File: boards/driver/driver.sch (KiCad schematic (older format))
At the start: 0 parts

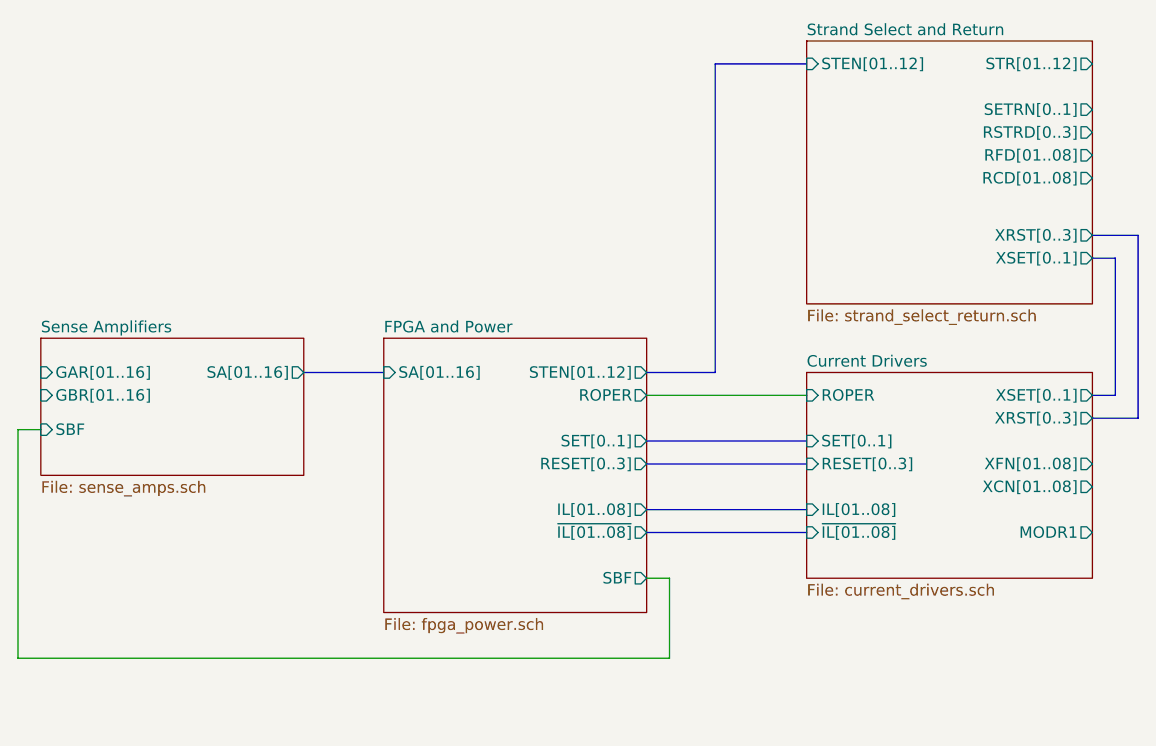
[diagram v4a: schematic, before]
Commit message: Completely overhauled rope driver circuitry to much, much more closely resemble the original.
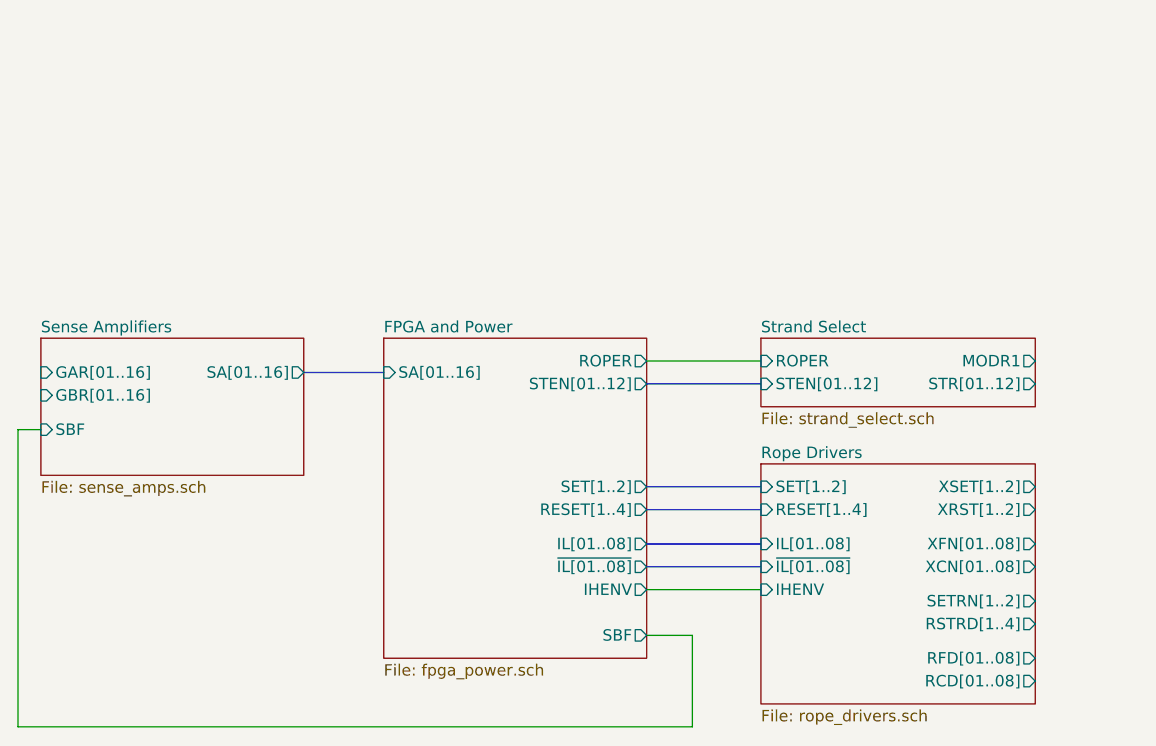
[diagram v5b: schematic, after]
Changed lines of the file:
@@
 $Descr USLedger 17000 11000
 encoding utf-8
-Sheet 1 5
+Sheet 1 68
 Title ""
 Date ""
@@
 F5 "SA[01..16]" O R 6950 3900 50
 $EndSheet
+Wire Bus Line
+	6950 3900 7300 3900
+Wire Wire Line
+	5700 4150 5800 4150
 $Sheet
-S 9150 2450 1250 1150
+S 8950 3750 1200 300
 U 64D2DF1E
-F0 "Strand Select and Return" 50
-F1 "strand_select_return.sch" 50
-F2 "STEN[01..12]" I L 9150 2550 50
-F3 "STR[01..12]" O R 10400 2550 50
-F4 "SETRN[0..1]" O R 10400 2750 50
-F5 "XSET[0..1]" O R 10400 3400 50
-F6 "RSTRD[0..3]" O R 10400 2850 50
-F7 "XRST[0..3]" O R 10400 3300 50
-F8 "RFD[01..08]" O R 10400 2950 50
-F9 "RCD[01..08]" O R 10400 3050 50
+F0 "Strand Select" 50
+F1 "strand_select.sch" 50
+F2 "STR[01..12]" O R 10150 3950 50
+F3 "ROPER" I L 8950 3850 50
+F4 "MODR1" O R 10150 3850 50
+F5 "STEN[01..12]" I L 8950 3950 50
 $EndSheet
 $Sheet
-S 9150 3900 1250 900
+S 8950 4300 1200 1050
 U 6183FAE6
-F0 "Current Drivers" 50
-F1 "current_drivers.sch" 50
-F2 "MODR1" O R 10400 4600 50
-F3 "ROPER" I L 9150 4000 50
-F4 "SET[0..1]" I L 9150 4200 50
-F5 "XSET[0..1]" O R 10400 4000 50
-F6 "RESET[0..3]" I L 9150 4300 50
-F7 "XRST[0..3]" O R 10400 4100 50
-F8 "~IL[01..08]" I L 9150 4600 50
-F9 "IL[01..08]" I L 9150 4500 50
-F10 "XFN[01..08]" O R 10400 4300 50
-F11 "XCN[01..08]" O R 10400 4400 50
+F0 "Rope Drivers" 50
+F1 "rope_drivers.sch" 50
+F2 "IHENV" I L 8950 4850 50
+F3 "SET[1..2]" I L 8950 4400 50
+F4 "RESET[1..4]" I L 8950 4500 50
+F5 "XRST[1..2]" O R 10150 4500 50
+F6 "XSET[1..2]" O R 10150 4400 50
+F7 "IL[01..08]" I L 8950 4650 50
+F8 "~IL[01..08]" I L 8950 4750 50
+F9 "XFN[01..08]" O R 10150 4650 50
+F10 "XCN[01..08]" O R 10150 4750 50
+F11 "RFD[01..08]" O R 10150 5150 50
+F12 "RCD[01..08]" O R 10150 5250 50
+F13 "SETRN[1..2]" O R 10150 4900 50
+F14 "RSTRD[1..4]" O R 10150 5000 50
 $EndSheet
+Wire Wire Line
+	8450 3850 8950 3850
 Wire Bus Line
-	10400 3300 10600 3300
-Wire Bus Line
-	10400 3400 10500 3400
-Wire Bus Line
-	10500 3400 10500 4000
-Wire Bus Line
-	10500 4000 10400 4000
+	8950 3950 8450 3950
 $Sheet
-S 7300 3750 1150 1200
+S 7300 3750 1150 1400
 U 652D8F7B
 F0 "FPGA and Power" 50
 F1 "fpga_power.sch" 50
 F2 "SA[01..16]" I L 7300 3900 50
-F3 "STEN[01..12]" O R 8450 3900 50
-F4 "SET[0..1]" O R 8450 4200 50
-F5 "RESET[0..3]" O R 8450 4300 50
-F6 "IL[01..08]" O R 8450 4500 50
-F7 "~IL[01..08]" O R 8450 4600 50
-F8 "ROPER" O R 8450 4000 50
-F9 "SBF" O R 8450 4800 50
+F3 "STEN[01..12]" O R 8450 3950 50
+F4 "SET[1..2]" O R 8450 4400 50
+F5 "RESET[1..4]" O R 8450 4500 50
+F6 "IL[01..08]" O R 8450 4650 50
+F7 "~IL[01..08]" O R 8450 4750 50
+F8 "ROPER" O R 8450 3850 50
+F9 "SBF" O R 8450 5050 50
+F10 "IHENV" O R 8450 4850 50
 $EndSheet
+Wire Wire Line
+	8450 4850 8950 4850
 Wire Bus Line
-	6950 3900 7300 3900
+	8450 4750 8950 4750
 Wire Bus Line
-	8450 3900 8750 3900
+	8950 4650 8450 4650
 Wire Bus Line
-	8750 3900 8750 2550
+	8450 4500 8950 4500
 Wire Bus Line
-	8750 2550 9150 2550
+	8950 4400 8450 4400
 Wire Wire Line
-	8450 4000 9150 4000
-Wire Bus Line
-	8450 4200 9150 4200
-Wire Bus Line
-	8450 4300 9150 4300
-Wire Bus Line
-	8450 4500 9150 4500
-Wire Bus Line
-	9150 4600 8450 4600
+	8450 5050 8650 5050
 Wire Wire Line
-	8450 4800 8550 4800
+	8650 5050 8650 5450
 Wire Wire Line
-	8550 4800 8550 5150
+	8650 5450 5700 5450
 Wire Wire Line
-	8550 5150 5700 5150
-Wire Wire Line
-	5700 5150 5700 4150
-Wire Wire Line
-	5700 4150 5800 4150
-Wire Bus Line
-	10400 4100 10600 4100
-Wire Bus Line
-	10600 3300 10600 4100
+	5700 4150 5700 5450
 $EndSCHEMATC

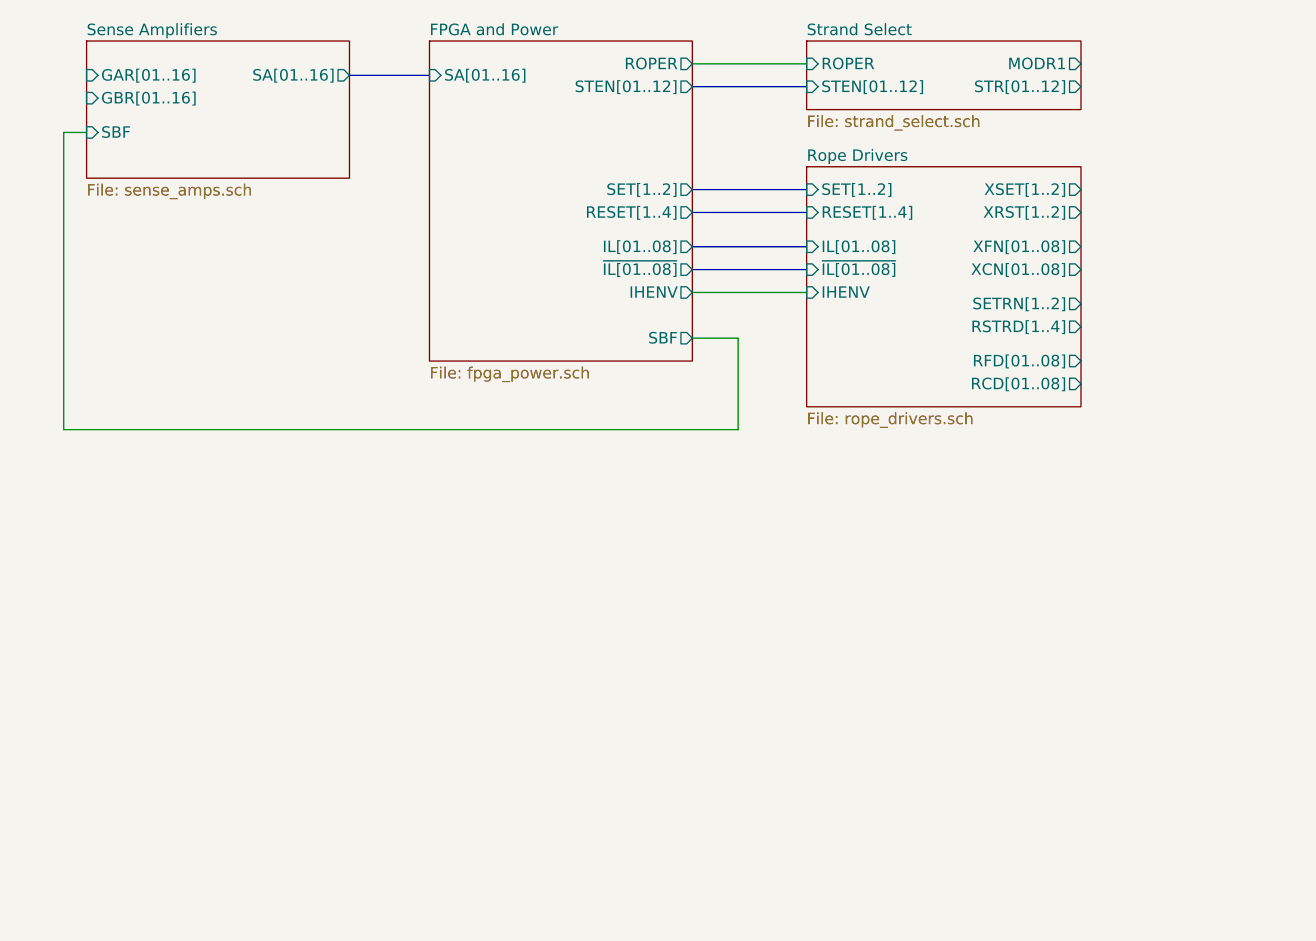
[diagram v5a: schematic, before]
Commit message: Driver board: finished first rough draft schematic. Lots of placeholders, but at least every place is held.
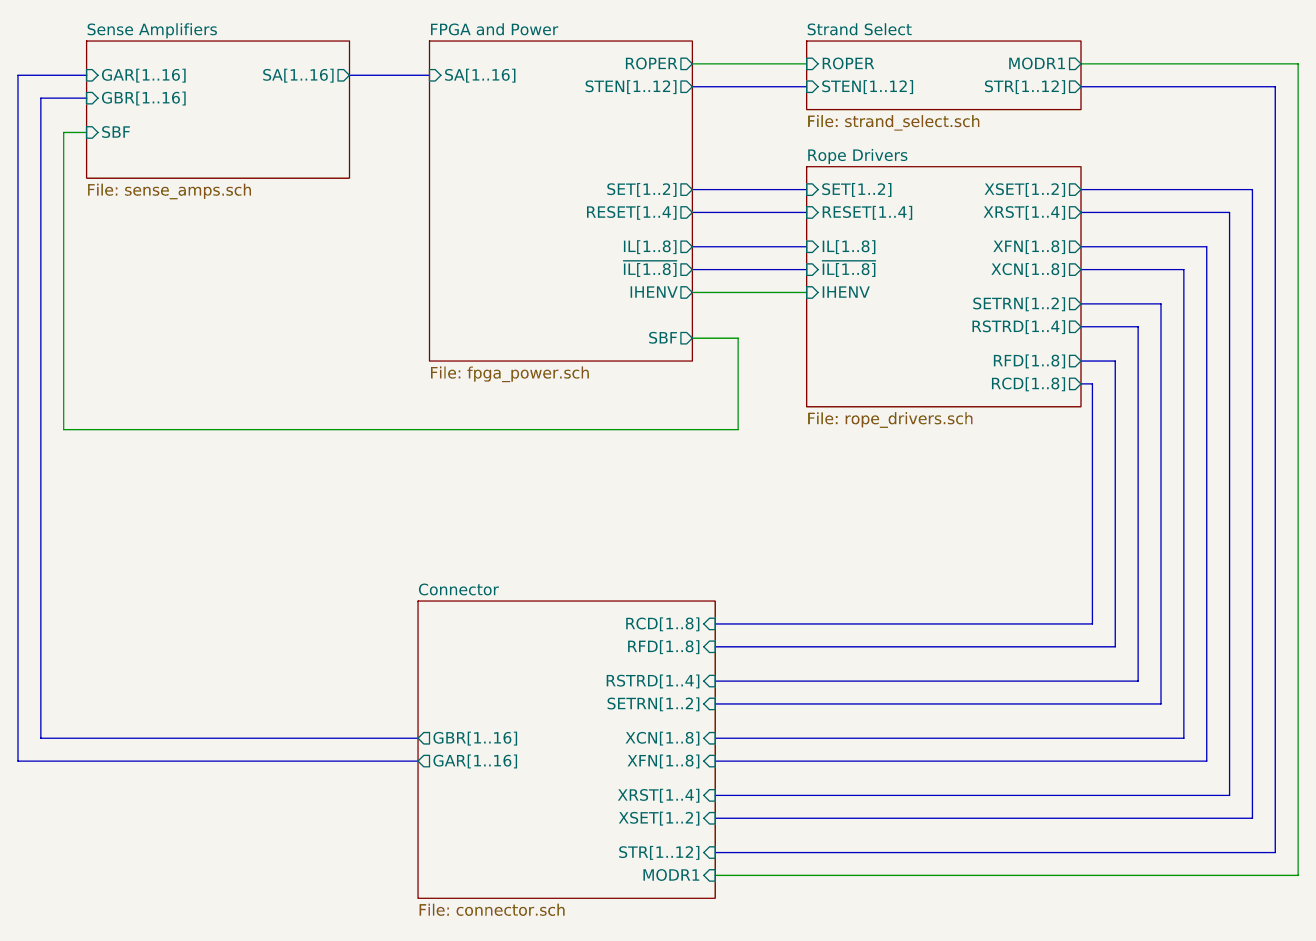
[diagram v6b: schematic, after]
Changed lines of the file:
@@
 $Descr USLedger 17000 11000
 encoding utf-8
-Sheet 1 68
+Sheet 1 69
 Title ""
 Date ""
@@
 F1 "sense_amps.sch" 50
 F2 "SBF" I L 5800 4150 50
-F3 "GAR[01..16]" I L 5800 3900 50
-F4 "GBR[01..16]" I L 5800 4000 50
-F5 "SA[01..16]" O R 6950 3900 50
+F3 "GAR[1..16]" I L 5800 3900 50
+F4 "GBR[1..16]" I L 5800 4000 50
+F5 "SA[1..16]" O R 6950 3900 50
 $EndSheet
 Wire Bus Line
@@
 F0 "Strand Select" 50
 F1 "strand_select.sch" 50
-F2 "STR[01..12]" O R 10150 3950 50
+F2 "STR[1..12]" O R 10150 3950 50
 F3 "ROPER" I L 8950 3850 50
 F4 "MODR1" O R 10150 3850 50
-F5 "STEN[01..12]" I L 8950 3950 50
+F5 "STEN[1..12]" I L 8950 3950 50
 $EndSheet
 $Sheet
@@
 F3 "SET[1..2]" I L 8950 4400 50
 F4 "RESET[1..4]" I L 8950 4500 50
-F5 "XRST[1..2]" O R 10150 4500 50
+F5 "XRST[1..4]" O R 10150 4500 50
 F6 "XSET[1..2]" O R 10150 4400 50
-F7 "IL[01..08]" I L 8950 4650 50
-F8 "~IL[01..08]" I L 8950 4750 50
-F9 "XFN[01..08]" O R 10150 4650 50
-F10 "XCN[01..08]" O R 10150 4750 50
-F11 "RFD[01..08]" O R 10150 5150 50
-F12 "RCD[01..08]" O R 10150 5250 50
+F7 "IL[1..8]" I L 8950 4650 50
+F8 "~IL[1..8]" I L 8950 4750 50
+F9 "XFN[1..8]" O R 10150 4650 50
+F10 "XCN[1..8]" O R 10150 4750 50
+F11 "RFD[1..8]" O R 10150 5150 50
+F12 "RCD[1..8]" O R 10150 5250 50
 F13 "SETRN[1..2]" O R 10150 4900 50
 F14 "RSTRD[1..4]" O R 10150 5000 50
@@
 F0 "FPGA and Power" 50
 F1 "fpga_power.sch" 50
-F2 "SA[01..16]" I L 7300 3900 50
-F3 "STEN[01..12]" O R 8450 3950 50
+F2 "SA[1..16]" I L 7300 3900 50
+F3 "STEN[1..12]" O R 8450 3950 50
 F4 "SET[1..2]" O R 8450 4400 50
 F5 "RESET[1..4]" O R 8450 4500 50
-F6 "IL[01..08]" O R 8450 4650 50
-F7 "~IL[01..08]" O R 8450 4750 50
+F6 "IL[1..8]" O R 8450 4650 50
+F7 "~IL[1..8]" O R 8450 4750 50
 F8 "ROPER" O R 8450 3850 50
 F9 "SBF" O R 8450 5050 50
@@
 Wire Wire Line
 	5700 4150 5700 5450
+$Sheet
+S 7250 6200 1300 1300
+U 61D45A0D
+F0 "Connector" 50
+F1 "connector.sch" 50
+F2 "GBR[1..16]" O L 7250 6800 50
+F3 "GAR[1..16]" O L 7250 6900 50
+F4 "XSET[1..2]" I R 8550 7150 50
+F5 "XRST[1..4]" I R 8550 7050 50
+F6 "XFN[1..8]" I R 8550 6900 50
+F7 "XCN[1..8]" I R 8550 6800 50
+F8 "MODR1" I R 8550 7400 50
+F9 "STR[1..12]" I R 8550 7300 50
+F10 "SETRN[1..2]" I R 8550 6650 50
+F11 "RSTRD[1..4]" I R 8550 6550 50
+F12 "RFD[1..8]" I R 8550 6400 50
+F13 "RCD[1..8]" I R 8550 6300 50
+$EndSheet
+Wire Bus Line
+	10150 5250 10200 5250
+Wire Bus Line
+	10200 5250 10200 6300
+Wire Bus Line
+	10200 6300 8550 6300
+Wire Bus Line
+	8550 6400 10300 6400
+Wire Bus Line
+	10300 6400 10300 5150
+Wire Bus Line
+	10300 5150 10150 5150
+Wire Bus Line
+	10150 5000 10400 5000
+Wire Bus Line
+	10400 5000 10400 6550
+Wire Bus Line
+	10400 6550 8550 6550
+Wire Bus Line
+	10150 4900 10500 4900
+Wire Bus Line
+	10500 4900 10500 6650
+Wire Bus Line
+	10500 6650 8550 6650
+Wire Bus Line
+	10150 4750 10600 4750
+Wire Bus Line
+	10600 4750 10600 6800
+Wire Bus Line
+	10600 6800 8550 6800
+Wire Bus Line
+	10150 4650 10700 4650
+Wire Bus Line
+	10700 4650 10700 6900
+Wire Bus Line
+	10700 6900 8550 6900
+Wire Bus Line
+	10150 4500 10800 4500
+Wire Bus Line
+	10800 4500 10800 7050
+Wire Bus Line
+	10800 7050 8550 7050
+Wire Bus Line
+	10150 4400 10900 4400
+Wire Bus Line
+	10900 4400 10900 7150
+Wire Bus Line
+	10900 7150 8550 7150
+Wire Bus Line
+	10150 3950 11000 3950
+Wire Bus Line
+	11000 3950 11000 7300
+Wire Bus Line
+	11000 7300 8550 7300
+Wire Wire Line
+	8550 7400 11100 7400
+Wire Wire Line
+	11100 7400 11100 3850
+Wire Wire Line
+	11100 3850 10150 3850
+Wire Bus Line
+	7250 6800 5600 6800
+Wire Bus Line
+	5600 6800 5600 4000
+Wire Bus Line
+	5600 4000 5800 4000
+Wire Bus Line
+	7250 6900 5500 6900
+Wire Bus Line
+	5500 6900 5500 3900
+Wire Bus Line
+	5500 3900 5800 3900
 $EndSCHEMATC

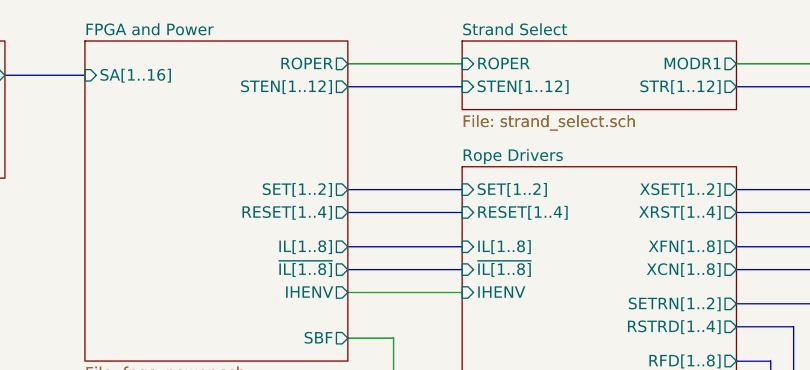
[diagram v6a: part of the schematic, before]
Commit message: Driver board: significant cleanup. Moved sense amp pairs into a subsheet, split tuning resistors into two globally, pushed input circuits into their corresponding sheets.
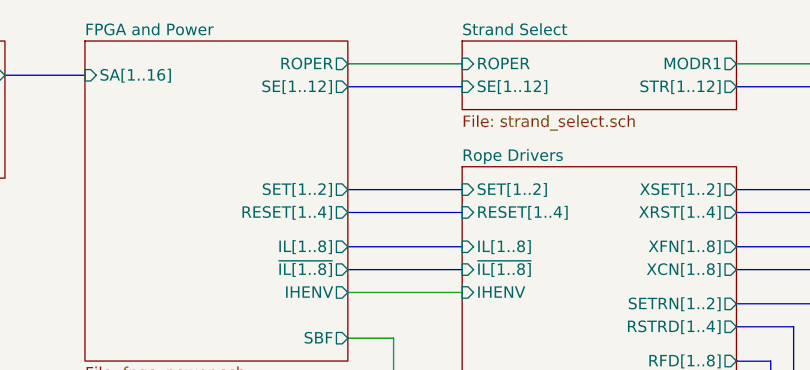
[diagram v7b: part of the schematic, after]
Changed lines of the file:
@@
 $Descr USLedger 17000 11000
 encoding utf-8
-Sheet 1 69
+Sheet 1 64
 Title ""
 Date ""
@@
 F3 "ROPER" I L 8950 3850 50
 F4 "MODR1" O R 10150 3850 50
-F5 "STEN[1..12]" I L 8950 3950 50
+F5 "SE[1..12]" I L 8950 3950 50
 $EndSheet
 $Sheet
@@
 F1 "fpga_power.sch" 50
 F2 "SA[1..16]" I L 7300 3900 50
-F3 "STEN[1..12]" O R 8450 3950 50
+F3 "SE[1..12]" O R 8450 3950 50
 F4 "SET[1..2]" O R 8450 4400 50
 F5 "RESET[1..4]" O R 8450 4500 50
